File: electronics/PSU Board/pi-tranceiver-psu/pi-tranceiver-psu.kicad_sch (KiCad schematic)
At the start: 28 parts, among them IC1 LTC4368IMS-2#PBF, Q1 DMT6002LPS-13, Q2 DMT6002LPS-13

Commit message: Re-upload conflicting files
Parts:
- added C?: 330uF, CAPAE660X770N, symbol SamacSys_Parts:865080545012
- added C? (x2): 10nF, Capacitor_SMD:C_1206_3216Metric_Pad1.33x1.80mm_HandSolder, symbol Device:C
- added C?: 100uF, CAPAE660X770N, symbol SamacSys_Parts:865080545012
- added C?: 100nF, Capacitor_SMD:C_1206_3216Metric_Pad1.33x1.80mm_HandSolder, symbol Device:C
- added D?: D_Schottky, symbol Device:D_Schottky
- added D?: 9.1V, Diode_SMD:D_0805_2012Metric, symbol Device:D_Zener
- added IC?: LM2679S-ADJ_NOPB, PSU_Board:TO127P1435X464-8N, symbol PSU_Board:LM2679S-ADJ_NOPB
- added J? (x5): JST 01x02, symbol Connector_Generic:Conn_01x02
- added J? (x6): Wago PCB 2 Pole, symbol Connector:Screw_Terminal_01x02
- added J?: JST 01x04, symbol Connector_Generic:Conn_01x04
- added JP?: 5.1V / 8.4V, symbol Jumper:Jumper_3_Bridged12
- added JP?: Jumper_2_Open, symbol Jumper:Jumper_2_Open
- added L?: 15uH, symbol Device:L_Ferrite
- added R?: 4K99, Resistor_SMD:R_0805_2012Metric_Pad1.20x1.40mm_HandSolder, symbol Device:R
- added R?: 5K9, Resistor_SMD:R_0805_2012Metric_Pad1.20x1.40mm_HandSolder, symbol Device:R
- added R?: 1K, Resistor_SMD:R_0805_2012Metric_Pad1.20x1.40mm_HandSolder, symbol Device:R
- added R?: 3K24, Resistor_SMD:R_0805_2012Metric_Pad1.20x1.40mm_HandSolder, symbol Device:R
- added R?: 100K, Resistor_SMD:R_0805_2012Metric_Pad1.20x1.40mm_HandSolder, symbol Device:R
- added U?: AMS1117-5.0, Package_TO_SOT_SMD:SOT-223-3_TabPin2, symbol Regulator_Linear:AMS1117-5.0
- C5: value 100uF -> 330uF
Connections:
- net GND: now also C?.2, C?.2, C?.2, C?.2, D?.2 (A), IC?.4 (GND), J?.1 (Pin_1), J?.2 (Pin_2), J?.2 (Pin_2), J?.2 (Pin_2), J?.2 (Pin_2), J?.2 (Pin_2), J?.2 (Pin_2), J?.2 (Pin_2), J?.2 (Pin_2), J?.2 (Pin_2), J?.2 (Pin_2), J?.2 (Pin_2), R?.2, R?.2, R?.2, U?.1 (GND)
- net at IC1.6 (~{SHDN}), R1.2: no longer Q?.1 (C)
- net at C3.1, C5.1, IC1.8 (VOUT)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: now also C?.1, D?.1 (K), IC?.2 (IN), J?.1 (Pin_1), J?.1 (Pin_1), J?.1 (Pin_1), J?.1 (Pin_1); no longer D?.2 (A)
- net at D?.2 (A): now also J?.4 (Pin_4)
- net at R?.1: now also D?.1 (K), SW?.2; no longer Q?.2 (B)
- net at Q?.1 (C), Q?.1 (G): now also R?.2; no longer R?.1
- net at Q?.3 (S), SW?.1, U?.3 (VI): now also R?.1, J?.1 (Pin_1); no longer R?.2
- net at D?.2 (A): now also J?.3 (Pin_3)
- net at D?.2 (A): now also J?.2 (Pin_2)
- net at C?.1, U?.2 (VO): now also J?.1 (Pin_1)
- net at D?.2 (A): now also J?.1 (Pin_1)
- new net: C?.1, J?.1 (Pin_1), J?.1 (Pin_1), J?.1 (Pin_1), JP?.1 (A), U?.2 (VO)
- new net: Q?.1 (C), Q?.2 (B), R?.1, R?.2
- new net: C?.1, J?.1 (Pin_1), JP?.2 (B), L?.1, R?.1, R?.1, U?.3 (VI)
- new net: JP?.1 (A), R?.2
- new net: IC?.6 (FB), JP?.2 (C), R?.1
- new net: JP?.3 (B), R?.2
- new net: IC?.5 (CURRENT_ADJ), R?.1
- new net: C?.1, IC?.7 (SS)
- new net: C?.1, D?.1 (K), IC?.1 (SW_OUT), L?.2
- new net: C?.2, IC?.3 (C_BOOST)
- new net: D?.2 (A), D?.2 (A)
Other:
- note added: "13.8V Output"
- note added: "5.1V @5A 8.4V @4A"
- note added: "Emergency Powerdown"
- note added: "Input"
- note added: "R_PI Shutdown"
- moved on the sheet: C1, C2, C3, C4, C5, C?, D1, D?, IC1, Q1, Q2, Q?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

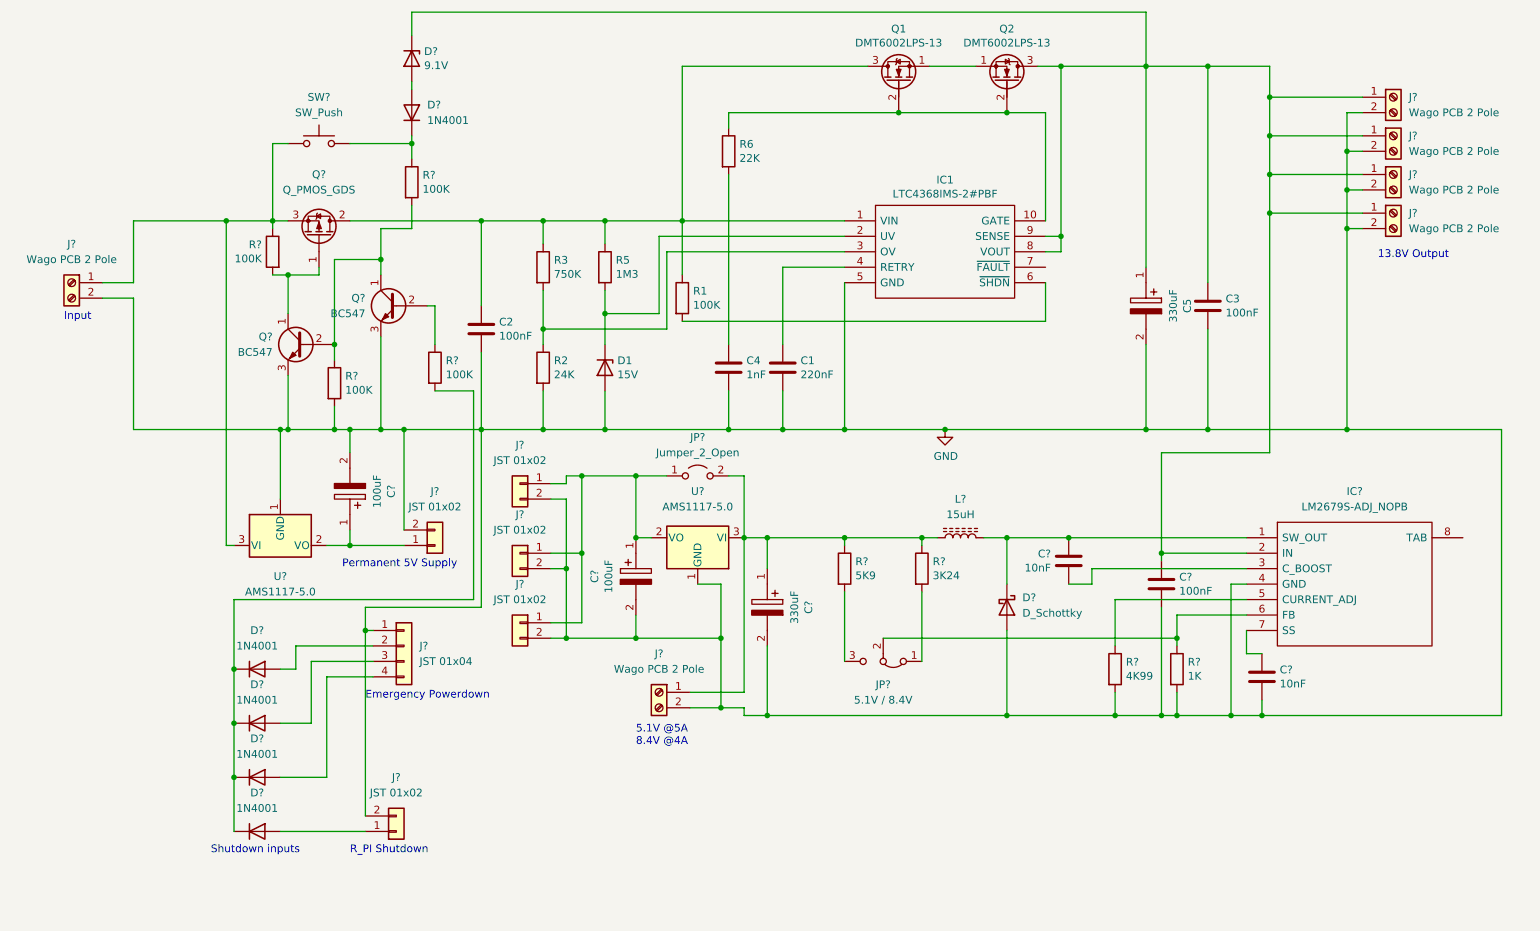
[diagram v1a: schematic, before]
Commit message: Added 5V Protection. Set component ID's
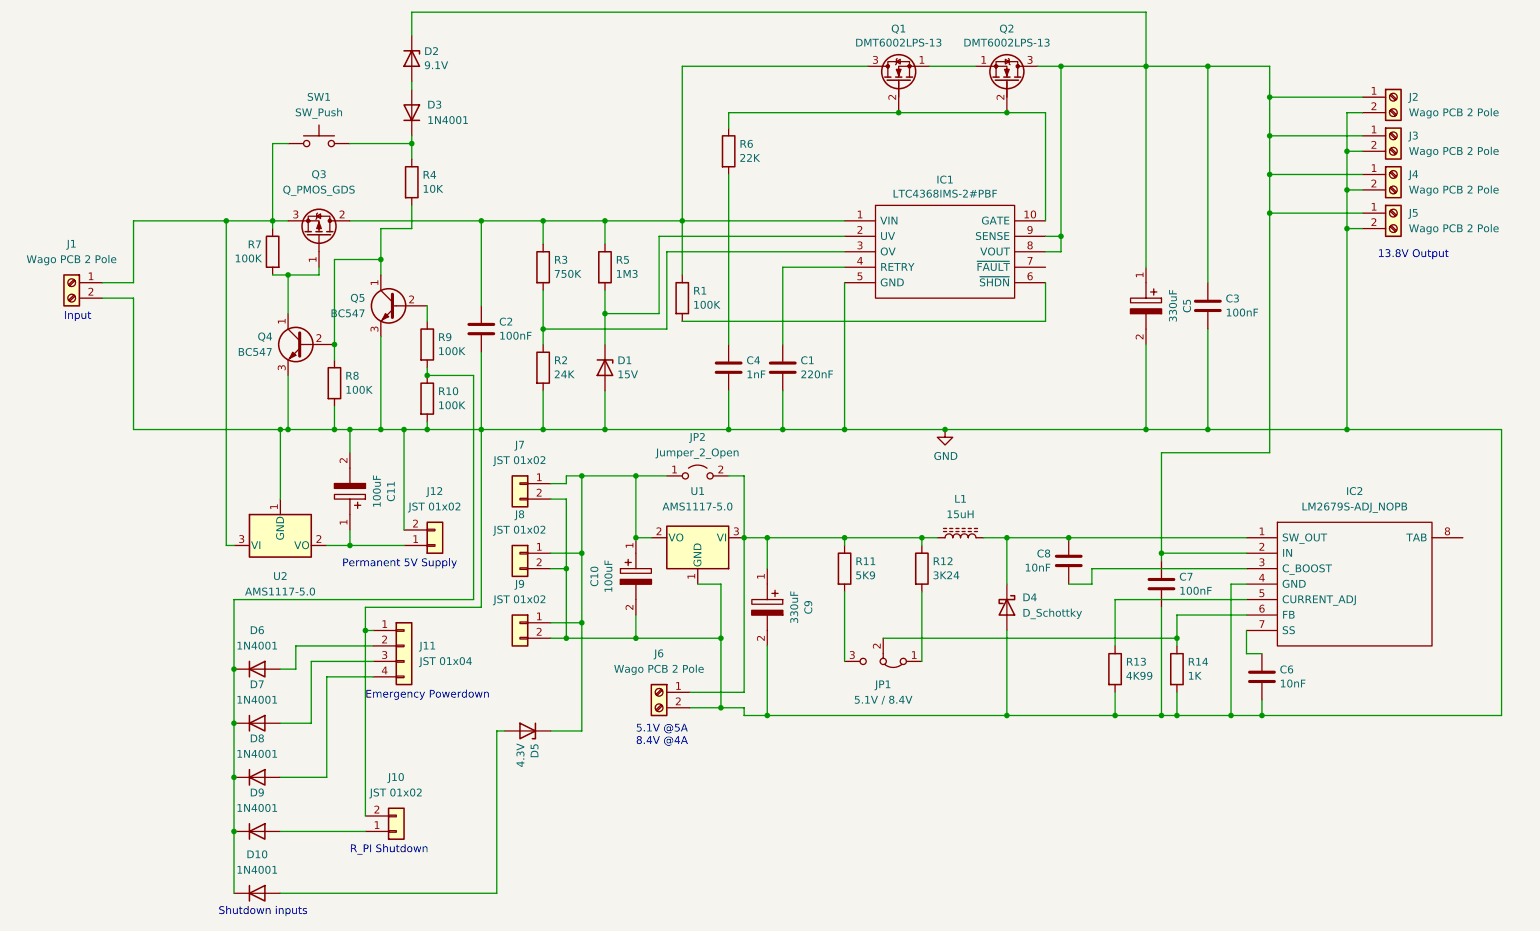
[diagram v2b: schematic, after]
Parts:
- added D10: 1N4001, Diode_THT:D_DO-41_SOD81_P10.16mm_Horizontal, symbol Diode:1N4001
- added D5: 4.3V, Diode_SMD:D_0805_2012Metric, symbol Device:D_Zener
- added R10: 100K, Resistor_SMD:R_0805_2012Metric_Pad1.20x1.40mm_HandSolder, symbol Device:R
- R4: renamed from R?; value 100K -> 10K
- gave numbers to parts that had none: 42
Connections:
- net GND: now also R10.2
- net at C10.1, J7.1 (Pin_1), J8.1 (Pin_1)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: now also D5.1 (K)
- net at D6.1 (K), D7.1 (K), D8.1 (K)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: now also D10.1 (K), R10.1
- new net: D10.2 (A), D5.2 (A)
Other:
- moved on the sheet: R9

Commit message: PCB Footprint Updates
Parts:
- C10, C11, C5: footprint CAPAE660X770N -> Capacitor_SMD:CP_Elec_6.3x4.5
- C9: footprint CAPAE660X770N -> Capacitor_SMD:CP_Elec_16x22
- IC1: footprint SOP50P490X110-10N -> PSU_Board:SOP50P490X110-10N
- L1: footprint (none) -> PSU_Board:SRP1265C-150M
- Q1, Q2: footprint SamacSys_Parts:PowerDI5060-8 -> PSU_Board:DMT6002LPS13
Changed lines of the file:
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@@
     (property "Reference" "IC1" (id 0) (at 173.99 44.069 0))
     (property "Value" "LTC4368IMS-2#PBF" (id 1) (at 173.99 46.3804 0))
-    (property "Footprint" "SOP50P490X110-10N" (id 2) (at 186.69 48.26 0)
+    (property "Footprint" "PSU_Board:SOP50P490X110-10N" (id 2) (at 186.69 48.26 0)
       (effects (font (size 1.27 1.27)) (justify left) hide)
     )
@@
     (property "Reference" "Q1" (id 0) (at 166.37 19.2532 90))
     (property "Value" "DMT6002LPS-13" (id 1) (at 166.37 21.5646 90))
-    (property "Footprint" "SamacSys_Parts:PowerDI5060-8" (id 2) (at 163.83 22.86 0)
+    (property "Footprint" "PSU_Board:DMT6002LPS13" (id 2) (at 163.83 22.86 0)
       (effects (font (size 1.27 1.27)) hide)
     )
@@
     (property "Reference" "Q2" (id 0) (at 184.15 19.2532 90))
     (property "Value" "DMT6002LPS-13" (id 1) (at 184.15 21.5646 90))
-    (property "Footprint" "SamacSys_Parts:PowerDI5060-8" (id 2) (at 186.69 22.86 0)
+    (property "Footprint" "PSU_Board:DMT6002LPS13" (id 2) (at 186.69 22.86 0)
       (effects (font (size 1.27 1.27)) hide)
     )
@@
     (property "Reference" "C5" (id 0) (at 213.7918 64.77 0))
     (property "Value" "330uF" (id 1) (at 211.4804 64.77 0))
-    (property "Footprint" "CAPAE660X770N" (id 2) (at 208.28 67.31 0)
+    (property "Footprint" "Capacitor_SMD:CP_Elec_6.3x4.5" (id 2) (at 208.28 67.31 0)
       (effects (font (size 1.27 1.27)) (justify left) hide)
     )
@@
     (property "Reference" "C9" (id 0) (at 151.5618 114.3 0))
     (property "Value" "330uF" (id 1) (at 149.2504 114.3 0))
-    (property "Footprint" "CAPAE660X770N" (id 2) (at 146.05 116.84 0)
+    (property "Footprint" "Capacitor_SMD:CP_Elec_16x22" (id 2) (at 146.05 116.84 0)
       (effects (font (size 1.27 1.27)) (justify left) hide)
     )
@@
     (property "Reference" "L1" (id 0) (at 176.53 96.52 90))
     (property "Value" "15uH" (id 1) (at 176.53 99.06 90))
-    (property "Footprint" "" (id 2) (at 176.53 102.87 0)
-      (effects (font (size 1.27 1.27)) hide)
-    )
-    (property "Datasheet" "https://www.mouser.co.uk/ProductDetail/Bourns/SRP1265C-150M?qs=OlC7AqGiEDnNYfbirifssw%3D%3D" (id 3) (at 176.53 102.87 0)
+    (property "Footprint" "PSU_Board:SRP1265C-150M" (id 2) (at 176.53 102.87 0)
+      (effects (font (size 1.27 1.27)) hide)
+    )
+    (property "Datasheet" "https://www.mouser.co.uk/ProductDetail/Bourns/SRP1265C-150M" (id 3) (at 176.53 102.87 0)
       (effects (font (size 1.27 1.27)) hide)
     )
@@
     (property "Reference" "C10" (id 0) (at 116.4082 109.22 0))
     (property "Value" "100uF" (id 1) (at 118.7196 109.22 0))
-    (property "Footprint" "CAPAE660X770N" (id 2) (at 121.92 111.76 0)
+    (property "Footprint" "Capacitor_SMD:CP_Elec_6.3x4.5" (id 2) (at 121.92 111.76 0)
       (effects (font (size 1.27 1.27)) (justify left) hide)
     )
@@
     (property "Reference" "C11" (id 0) (at 82.9818 95.25 0))
     (property "Value" "100uF" (id 1) (at 80.6704 95.25 0))
-    (property "Footprint" "CAPAE660X770N" (id 2) (at 77.47 92.71 0)
+    (property "Footprint" "Capacitor_SMD:CP_Elec_6.3x4.5" (id 2) (at 77.47 92.71 0)
       (effects (font (size 1.27 1.27)) (justify left) hide)
     )
@@
     )
     (path "/00000000-0000-0000-0000-00006120d999"
-      (reference "C5") (unit 1) (value "330uF") (footprint "CAPAE660X770N")
+      (reference "C5") (unit 1) (value "330uF") (footprint "Capacitor_SMD:CP_Elec_6.3x4.5")
     )
     (path "/499e6dbe-afef-4741-a182-f5eb5809beb2"
@@
     )
     (path "/2d25826c-159a-420f-bd15-081a9746af2b"
-      (reference "C9") (unit 1) (value "330uF") (footprint "CAPAE660X770N")
+      (reference "C9") (unit 1) (value "330uF") (footprint "Capacitor_SMD:CP_Elec_16x22")
     )
     (path "/8f32af4f-847c-4a57-92a0-c9818043d538"
-      (reference "C10") (unit 1) (value "100uF") (footprint "CAPAE660X770N")
+      (reference "C10") (unit 1) (value "100uF") (footprint "Capacitor_SMD:CP_Elec_6.3x4.5")
     )
     (path "/bae8ec93-951f-4399-932d-4c08dd039d22"
-      (reference "C11") (unit 1) (value "100uF") (footprint "CAPAE660X770N")
+      (reference "C11") (unit 1) (value "100uF") (footprint "Capacitor_SMD:CP_Elec_6.3x4.5")
     )
     (path "/00000000-0000-0000-0000-00006165a556"
@@
     )
     (path "/00000000-0000-0000-0000-0000611e624f"
-      (reference "IC1") (unit 1) (value "LTC4368IMS-2#PBF") (footprint "SOP50P490X110-10N")
+      (reference "IC1") (unit 1) (value "LTC4368IMS-2#PBF") (footprint "PSU_Board:SOP50P490X110-10N")
     )
     (path "/a5204756-7f86-40f2-a652-9dbcca1ec2c0"
@@
     )
     (path "/65589fd2-ba2d-4505-8223-5e5d9ec2194b"
-      (reference "L1") (unit 1) (value "15uH") (footprint "")
+      (reference "L1") (unit 1) (value "15uH") (footprint "PSU_Board:SRP1265C-150M")
     )
     (path "/00000000-0000-0000-0000-0000611fa833"
-      (reference "Q1") (unit 1) (value "DMT6002LPS-13") (footprint "SamacSys_Parts:PowerDI5060-8")
+      (reference "Q1") (unit 1) (value "DMT6002LPS-13") (footprint "PSU_Board:DMT6002LPS13")
     )
     (path "/00000000-0000-0000-0000-0000611fe1c6"
-      (reference "Q2") (unit 1) (value "DMT6002LPS-13") (footprint "SamacSys_Parts:PowerDI5060-8")
+      (reference "Q2") (unit 1) (value "DMT6002LPS-13") (footprint "PSU_Board:DMT6002LPS13")
     )
     (path "/ede81877-ee59-4b3f-9383-28f6e70df317"
